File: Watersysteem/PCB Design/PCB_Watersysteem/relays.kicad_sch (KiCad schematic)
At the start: 43 parts, among them J14 Pomp1, J15 Pomp2, J16 Pomp3, J17 Pomp4, J18 Luchtpomp, J19 Mixer, J20 UV, J22 230V, K1 AHQSS105DM2FA0G, K2 AHQSS105DM2FA0G, K3 AHQSS105DM2FA0G, K6 AHQSS105DM2FA0G, K7 AHQSS105DM2FA0G, K8 AHQSS105DM2FA0G, K9 AHQSS105DM2FA0G, Q1 BC817, Q2 BC817, Q3 BC817, Q4 BC817, Q5 BC817, Q6 BC817, Q7 BC817

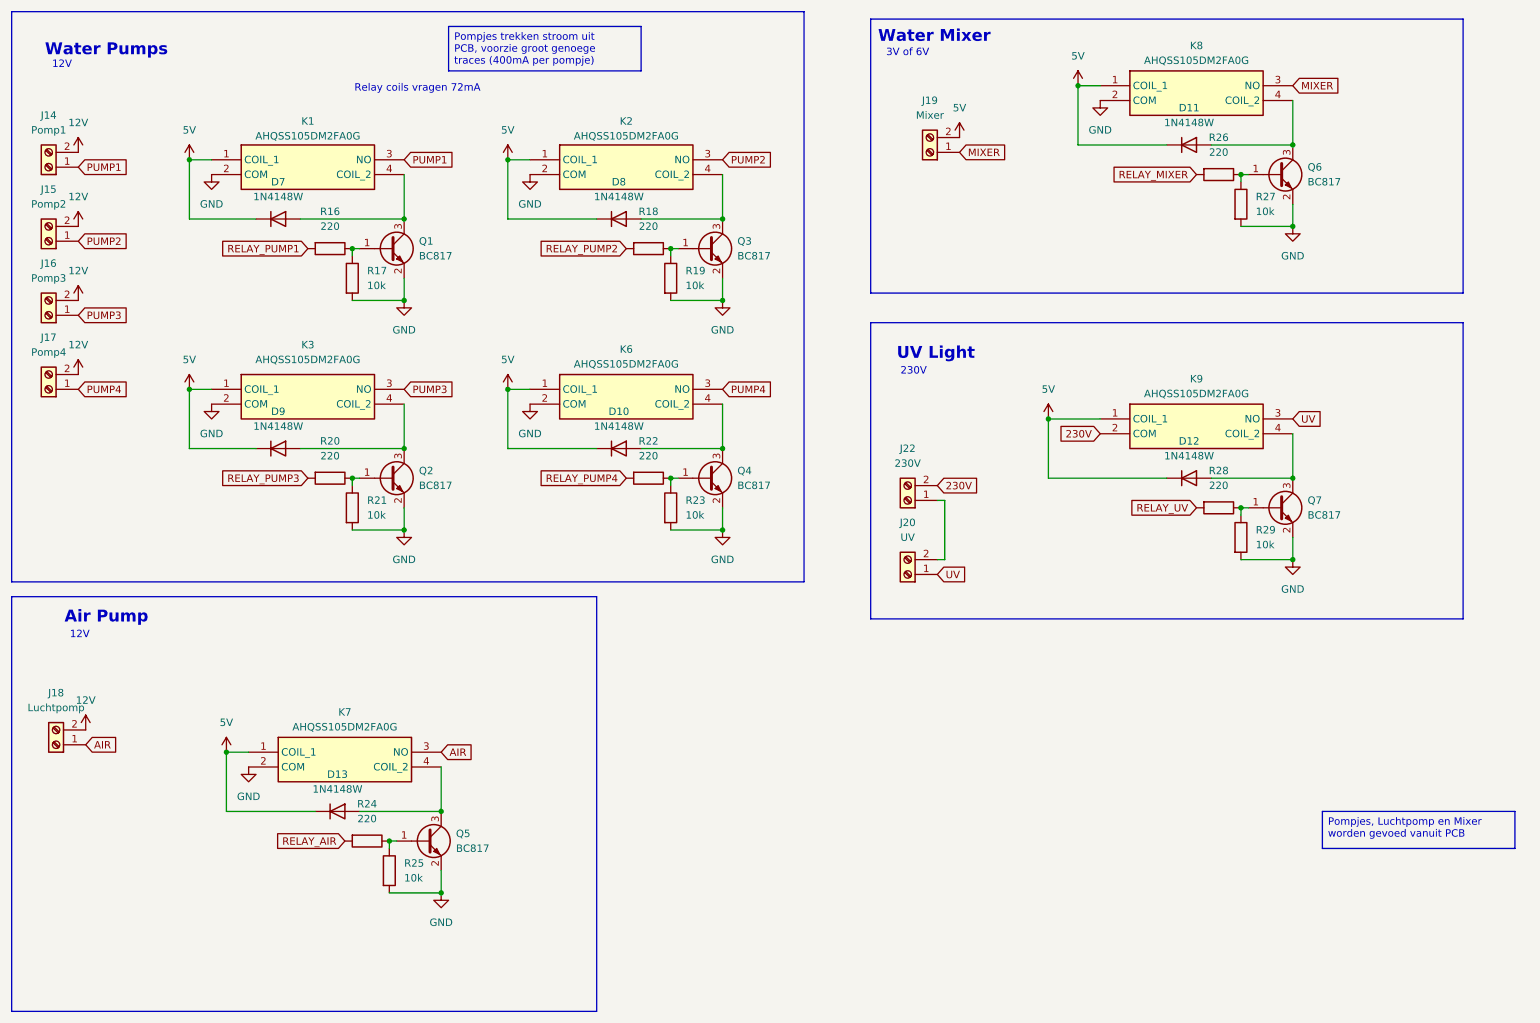
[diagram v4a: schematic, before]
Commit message: Update PCB
transistoren vervangen door mosfets
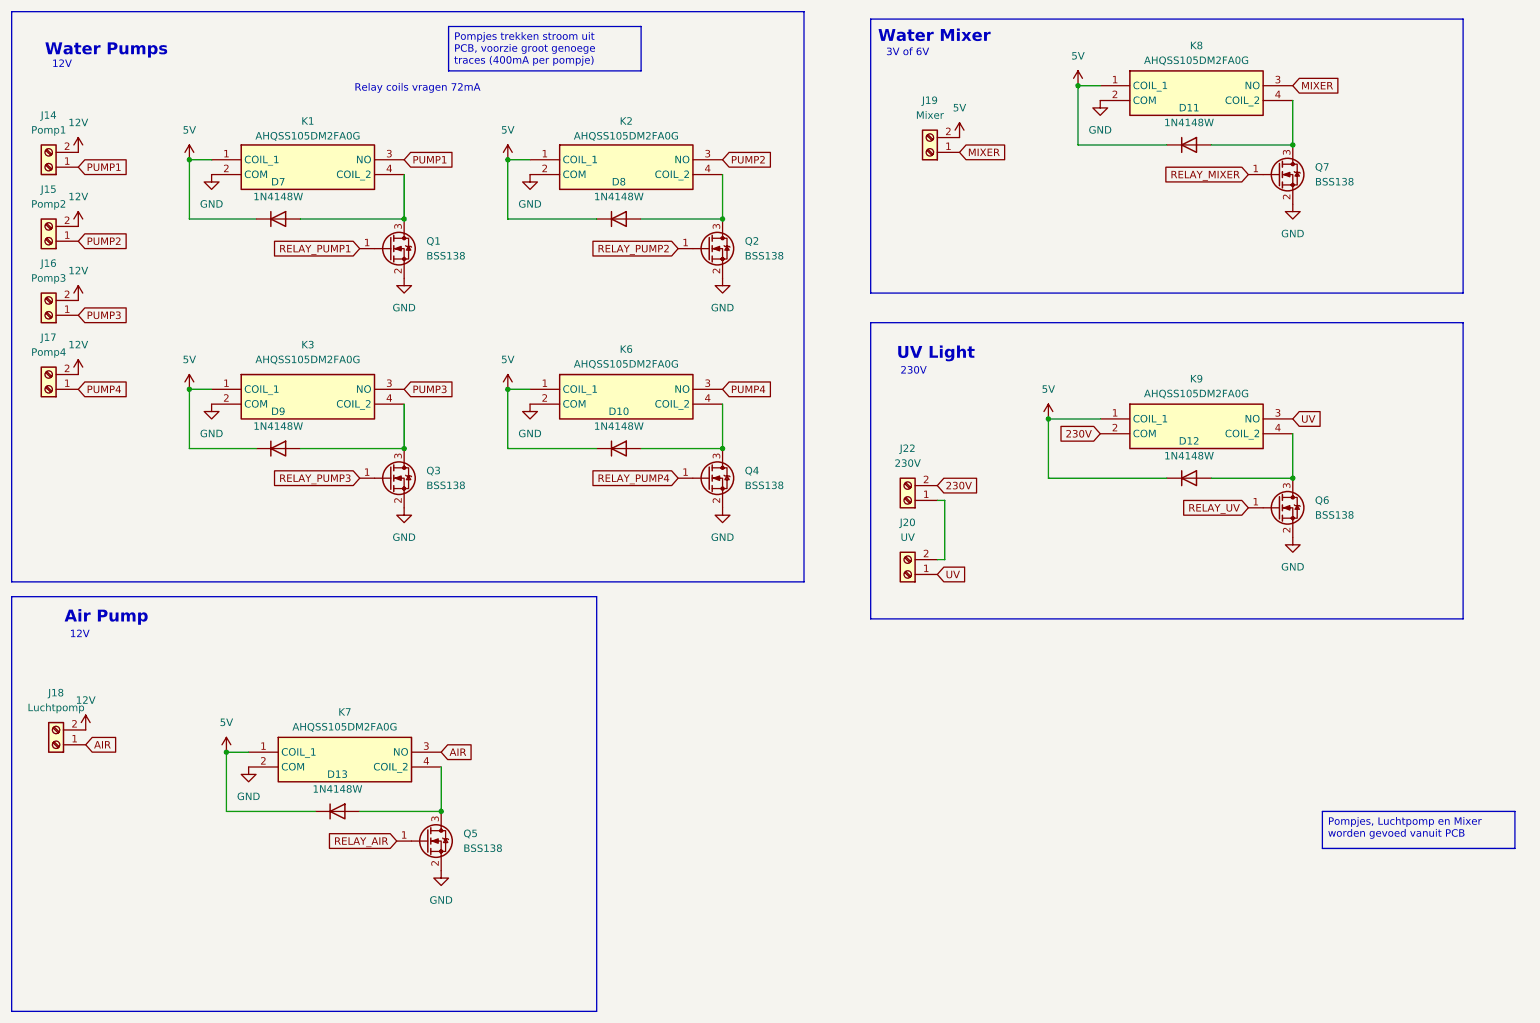
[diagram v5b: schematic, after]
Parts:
- removed Q1, Q2, Q3, Q4, Q5, Q6, Q7: BC817, Package_TO_SOT_SMD:SOT-23, symbol Transistor_BJT:BC817
- removed R16, R18, R20, R22, R24, R26, R28: 220, Resistor_SMD:R_0805_2012Metric_Pad1.20x1.40mm_HandSolder, symbol Device:R
- removed R17, R19, R21, R23, R25, R27, R29: 10k, Resistor_SMD:R_0805_2012Metric_Pad1.20x1.40mm_HandSolder, symbol Device:R
- added Q1, Q2, Q3, Q4, Q5, Q6, Q7: BSS138, Package_TO_SOT_SMD:SOT-23, symbol Transistor_FET:BSS138
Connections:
- net GND: now also Q1.2 (S), Q2.2 (S), Q3.2 (S), Q4.2 (S), Q5.2 (S), Q6.2 (S), Q7.2 (S)
- net RELAY_AIR: now also Q5.1 (G)
- net RELAY_MIXER: now also Q7.1 (G)
- net RELAY_PUMP1: now also Q1.1 (G)
- net RELAY_PUMP2: now also Q2.1 (G)
- net RELAY_PUMP3: now also Q3.1 (G)
- net RELAY_PUMP4: now also Q4.1 (G)
- net RELAY_UV: now also Q6.1 (G)
- net at D13.2 (A), K7.4 (COIL_2): now also Q5.3 (D)
- net at D8.2 (A), K2.4 (COIL_2): now also Q2.3 (D)
- net at D11.2 (A), K8.4 (COIL_2): now also Q7.3 (D)
- net at D12.2 (A), K9.4 (COIL_2): now also Q6.3 (D)
- net at D7.2 (A), K1.4 (COIL_2): now also Q1.3 (D)
- net at D10.2 (A), K6.4 (COIL_2): now also Q4.3 (D)
- net at D9.2 (A), K3.4 (COIL_2): now also Q3.3 (D)

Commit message: Update PCB
IO gemapt, Condensator ADC, Schematic geprint
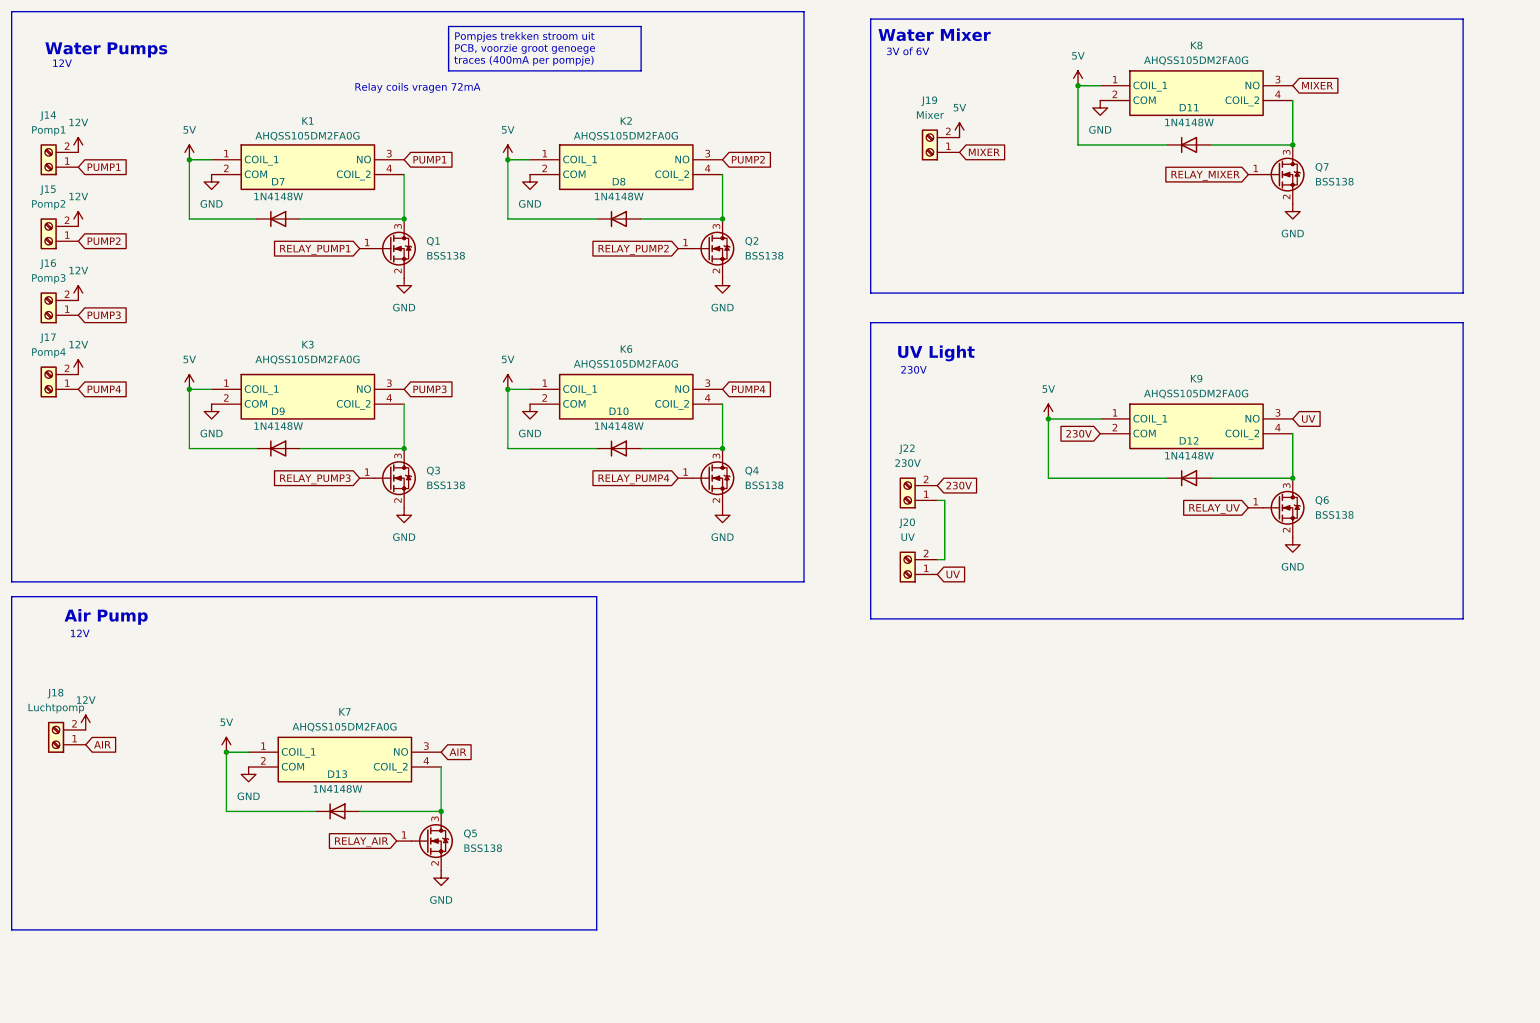
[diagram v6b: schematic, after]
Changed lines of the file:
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@@
 	(rectangle
 		(start 20.32 116.84)
-		(end 120.65 187.96)
+		(end 120.65 173.99)
 		(stroke
 			(width 0)
@@
 		(margins 0.9525 0.9525 0.9525 0.9525)
 		(stroke
-			(width 0)
-			(type default)
-		)
-		(fill
-			(type none)
-		)
-		(effects
-			(font
-				(size 1.27 1.27)
-			)
-			(justify left top)
-		)
-	)
-	(text_box "Pompjes, Luchtpomp en Mixer worden gevoed vanuit PCB"
-		(exclude_from_sim no)
-		(at 245.11 153.67 0)
-		(size 33.02 6.35)
-		(margins 0.9525 0.9525 0.9525 0.9525)
-		(stroke

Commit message: Update PCB
alle footprints staan correct, alles in PCB geïmporteert
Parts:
- J14, J15, J16, J17, J18, J19, J20, J22: footprint (none) -> TerminalBlock_Phoenix:TerminalBlock_Phoenix_PT-1,5-2-5.0-H_1x02_P5.00mm_Horizontal
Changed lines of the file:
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@@
 			)
 		)
-		(property "Footprint" ""
+		(property "Footprint" "TerminalBlock_Phoenix:TerminalBlock_Phoenix_PT-1,5-2-5.0-H_1x02_P5.00mm_Horizontal"
 			(at 27.94 142.24 0)
 			(effects
@@
 			)
 		)
-		(property "Footprint" ""
+		(property "Footprint" "TerminalBlock_Phoenix:TerminalBlock_Phoenix_PT-1,5-2-5.0-H_1x02_P5.00mm_Horizontal"
 			(at 177.8 40.64 0)
 			(effects
@@
 			)
 		)
-		(property "Footprint" ""
+		(property "Footprint" "TerminalBlock_Phoenix:TerminalBlock_Phoenix_PT-1,5-2-5.0-H_1x02_P5.00mm_Horizontal"
 			(at 26.67 68.58 0)
 			(effects
@@
 			)
 		)
-		(property "Footprint" ""
+		(property "Footprint" "TerminalBlock_Phoenix:TerminalBlock_Phoenix_PT-1,5-2-5.0-H_1x02_P5.00mm_Horizontal"
 			(at 26.67 81.28 0)
 			(effects
@@
 			)
 		)
-		(property "Footprint" ""
+		(property "Footprint" "TerminalBlock_Phoenix:TerminalBlock_Phoenix_PT-1,5-2-5.0-H_1x02_P5.00mm_Horizontal"
 			(at 26.67 43.18 0)
 			(effects
@@
 			)
 		)
-		(property "Footprint" ""
+		(property "Footprint" "TerminalBlock_Phoenix:TerminalBlock_Phoenix_PT-1,5-2-5.0-H_1x02_P5.00mm_Horizontal"
 			(at 173.99 113.03 0)
 			(effects
@@
 			)
 		)
-		(property "Footprint" ""
+		(property "Footprint" "TerminalBlock_Phoenix:TerminalBlock_Phoenix_PT-1,5-2-5.0-H_1x02_P5.00mm_Horizontal"
 			(at 26.67 55.88 0)
 			(effects
@@
 			)
 		)
-		(property "Footprint" ""
+		(property "Footprint" "TerminalBlock_Phoenix:TerminalBlock_Phoenix_PT-1,5-2-5.0-H_1x02_P5.00mm_Horizontal"
 			(at 173.99 100.33 0)
 			(effects

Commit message: Update PCB
Afmetingen verkleind (100x100), rerouting, clean-up
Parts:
- renumbered D13 to D10, D7 to D4, D8 to D5, D9 to D6, D12 to D7, D11 to D8, D10 to D9, J15 to J12, J18 to J20, J19 to J22, J22 to J23, J20 to J24, J14 to J6, K6 to K4, K8 to K5, K9 to K6, Q6 to Q4, Q7 to Q5, Q4 to Q6, Q5 to Q7
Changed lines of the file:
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@@
 		(dnp no)
 		(fields_autoplaced yes)
-		(property "Reference" "J18"
+		(property "Reference" "J20"
 			(at 27.94 133.35 0)
 			(effects
@@
 			(project "PCB_Watersysteem"
 				(path "/de0b8b90-8fde-4ab1-b1b1-e85d44454ecd/9d362e6d-9323-41d2-ab33-f0630b5b7c79"
-					(reference "J18")
+					(reference "J20")
 					(unit 1)
 				)
@@
 		(dnp no)
 		(fields_autoplaced yes)
-		(property "Reference" "D13"
+		(property "Reference" "D10"
 			(at 76.2 147.32 0)
 			(effects
@@
 			(project "PCB_Watersysteem"
 				(path "/de0b8b90-8fde-4ab1-b1b1-e85d44454ecd/9d362e6d-9323-41d2-ab33-f0630b5b7c79"
-					(reference "D13")
+					(reference "D10")
 					(unit 1)
 				)
@@
 		(dnp no)
 		(fields_autoplaced yes)
-		(property "Reference" "Q7"
+		(property "Reference" "Q5"
 			(at 243.84 43.1799 0)
 			(effects
@@
 			(project "PCB_Watersysteem"
 				(path "/de0b8b90-8fde-4ab1-b1b1-e85d44454ecd/9d362e6d-9323-41d2-ab33-f0630b5b7c79"
-					(reference "Q7")
+					(reference "Q5")
 					(unit 1)
 				)
@@
 		(dnp no)
 		(fields_autoplaced yes)
-		(property "Reference" "Q4"
+		(property "Reference" "Q6"
 			(at 146.05 95.2499 0)
 			(effects
@@
 			(project "PCB_Watersysteem"
 				(path "/de0b8b90-8fde-4ab1-b1b1-e85d44454ecd/9d362e6d-9323-41d2-ab33-f0630b5b7c79"
-					(reference "Q4")
+					(reference "Q6")
 					(unit 1)
 				)
@@
 		(dnp no)
 		(fields_autoplaced yes)
-		(property "Reference" "J19"
+		(property "Reference" "J22"
 			(at 177.8 31.75 0)
 			(effects
@@
 			(project "PCB_Watersysteem"
 				(path "/de0b8b90-8fde-4ab1-b1b1-e85d44454ecd/9d362e6d-9323-41d2-ab33-f0630b5b7c79"
-					(reference "J19")
+					(reference "J22")
 					(unit 1)
 				)
@@
 		(dnp no)
 		(fields_autoplaced yes)
-		(property "Reference" "D12"
+		(property "Reference" "D7"
 			(at 222.25 90.17 0)
 			(effects
@@
 			(project "PCB_Watersysteem"
 				(path "/de0b8b90-8fde-4ab1-b1b1-e85d44454ecd/9d362e6d-9323-41d2-ab33-f0630b5b7c79"
-					(reference "D12")
+					(reference "D7")
 					(unit 1)
 				)
@@
 		(on_board yes)
 		(dnp no)
-		(property "Reference" "K8"
+		(property "Reference" "K5"
 			(at 223.52 22.352 0)
 			(effects
@@
 			(project "PCB_Watersysteem"
 				(path "/de0b8b90-8fde-4ab1-b1b1-e85d44454ecd/9d362e6d-9323-41d2-ab33-f0630b5b7c79"
-					(reference "K8")
+					(reference "K5")
 					(unit 1)
 				)
@@
 		(dnp no)
 		(fields_autoplaced yes)
-		(property "Reference" "D10"
+		(property "Reference" "D9"
 			(at 124.46 85.09 0)
 			(effects
@@
 			(project "PCB_Watersysteem"
 				(path "/de0b8b90-8fde-4ab1-b1b1-e85d44454ecd/9d362e6d-9323-41d2-ab33-f0630b5b7c79"
-					(reference "D10")
+					(reference "D9")
 					(unit 1)
 				)
@@
 		(dnp no)
 		(fields_autoplaced yes)
-		(property "Reference" "D8"
+		(property "Reference" "D5"
 			(at 124.46 45.72 0)
 			(effects
@@
 			(project "PCB_Watersysteem"
 				(path "/de0b8b90-8fde-4ab1-b1b1-e85d44454ecd/9d362e6d-9323-41d2-ab33-f0630b5b7c79"
-					(reference "D8")
+					(reference "D5")
 					(unit 1)
 				)
@@
 		(dnp no)
 		(fields_autoplaced yes)
-		(property "Reference" "J14"
+		(property "Reference" "J6"
 			(at 26.67 34.29 0)
 			(effects
@@
 			(project ""
 				(path "/de0b8b90-8fde-4ab1-b1b1-e85d44454ecd/9d362e6d-9323-41d2-ab33-f0630b5b7c79"
-					(reference "J14")
+					(reference "J6")
 					(unit 1)
 				)
@@
 		(dnp no)
 		(fields_autoplaced yes)
-		(property "Reference" "J20"
+		(property "Reference" "J24"
 			(at 173.99 104.14 0)
 			(effects
@@
 			(project "PCB_Watersysteem"
 				(path "/de0b8b90-8fde-4ab1-b1b1-e85d44454ecd/9d362e6d-9323-41d2-ab33-f0630b5b7c79"
-					(reference "J20")
+					(reference "J24")
 					(unit 1)
 				)
@@
 		(on_board yes)
 		(dnp no)
-		(property "Reference" "K9"
+		(property "Reference" "K6"
 			(at 223.52 79.502 0)
 			(effects
@@
 			(project "PCB_Watersysteem"
 				(path "/de0b8b90-8fde-4ab1-b1b1-e85d44454ecd/9d362e6d-9323-41d2-ab33-f0630b5b7c79"
-					(reference "K9")
+					(reference "K6")
 					(unit 1)
 				)
@@
 		(dnp no)
 		(fields_autoplaced yes)
-		(property "Reference" "J15"
+		(property "Reference" "J12"
 			(at 26.67 46.99 0)
 			(effects
@@
 			(project "PCB_Watersysteem"
 				(path "/de0b8b90-8fde-4ab1-b1b1-e85d44454ecd/9d362e6d-9323-41d2-ab33-f0630b5b7c79"
-					(reference "J15")
+					(reference "J12")
 					(unit 1)
 				)
@@
 		(on_board yes)
 		(dnp no)
-		(property "Reference" "K6"
+		(property "Reference" "K4"
 			(at 125.73 74.422 0)
 			(effects
@@
 			(project "PCB_Watersysteem"
 				(path "/de0b8b90-8fde-4ab1-b1b1-e85d44454ecd/9d362e6d-9323-41d2-ab33-f0630b5b7c79"
-					(reference "K6")
+					(reference "K4")
 					(unit 1)
 				)
@@
 		(dnp no)
 		(fields_autoplaced yes)
-		(property "Reference" "D7"
+		(property "Reference" "D4"
 			(at 66.04 45.72 0)
 			(effects
@@
 			(project ""
 				(path "/de0b8b90-8fde-4ab1-b1b1-e85d44454ecd/9d362e6d-9323-41d2-ab33-f0630b5b7c79"
-					(reference "D7")
+					(reference "D4")
 					(unit 1)
 				)
@@
 		(dnp no)
 		(fields_autoplaced yes)
-		(property "Reference" "Q6"
+		(property "Reference" "Q4"
 			(at 243.84 100.3299 0)
 			(effects
@@
 			(project "PCB_Watersysteem"
 				(path "/de0b8b90-8fde-4ab1-b1b1-e85d44454ecd/9d362e6d-9323-41d2-ab33-f0630b5b7c79"
-					(reference "Q6")
+					(reference "Q4")
 					(unit 1)
 				)
@@
 		(dnp no)
 		(fields_autoplaced yes)
-		(property "Reference" "D11"
+		(property "Reference" "D8"
 			(at 222.25 33.02 0)
 			(effects
@@
 			(project "PCB_Watersysteem"
 				(path "/de0b8b90-8fde-4ab1-b1b1-e85d44454ecd/9d362e6d-9323-41d2-ab33-f0630b5b7c79"
-					(reference "D11")
+					(reference "D8")
 					(unit 1)
 				)
@@
 		(dnp no)
 		(fields_autoplaced yes)
-		(property "Reference" "D9"
+		(property "Reference" "D6"
 			(at 66.04 85.09 0)
 			(effects
@@
 			(project "PCB_Watersysteem"
 				(path "/de0b8b90-8fde-4ab1-b1b1-e85d44454ecd/9d362e6d-9323-41d2-ab33-f0630b5b7c79"
-					(reference "D9")
+					(reference "D6")
 					(unit 1)
 				)
@@
 		(dnp no)
 		(fields_autoplaced yes)
-		(property "Reference" "Q5"
+		(property "Reference" "Q7"
 			(at 97.79 157.4799 0)
 			(effects
@@
 			(project "PCB_Watersysteem"
 				(path "/de0b8b90-8fde-4ab1-b1b1-e85d44454ecd/9d362e6d-9323-41d2-ab33-f0630b5b7c79"
-					(reference "Q5")
+					(reference "Q7")
 					(unit 1)
 				)
@@
 		(dnp no)
 		(fields_autoplaced yes)
-		(property "Reference" "J22"
+		(property "Reference" "J23"
 			(at 173.99 91.44 0)
 			(effects
@@
 			(project "PCB_Watersysteem"
 				(path "/de0b8b90-8fde-4ab1-b1b1-e85d44454ecd/9d362e6d-9323-41d2-ab33-f0630b5b7c79"
-					(reference "J22")
+					(reference "J23")
 					(unit 1)
 				)
